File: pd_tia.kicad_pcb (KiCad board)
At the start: 2 copper layers, 75.1 x 65.2 mm, 21 parts, among them P1 BNC, U1 ED2610, U2 LM2940, U3 OPA2211

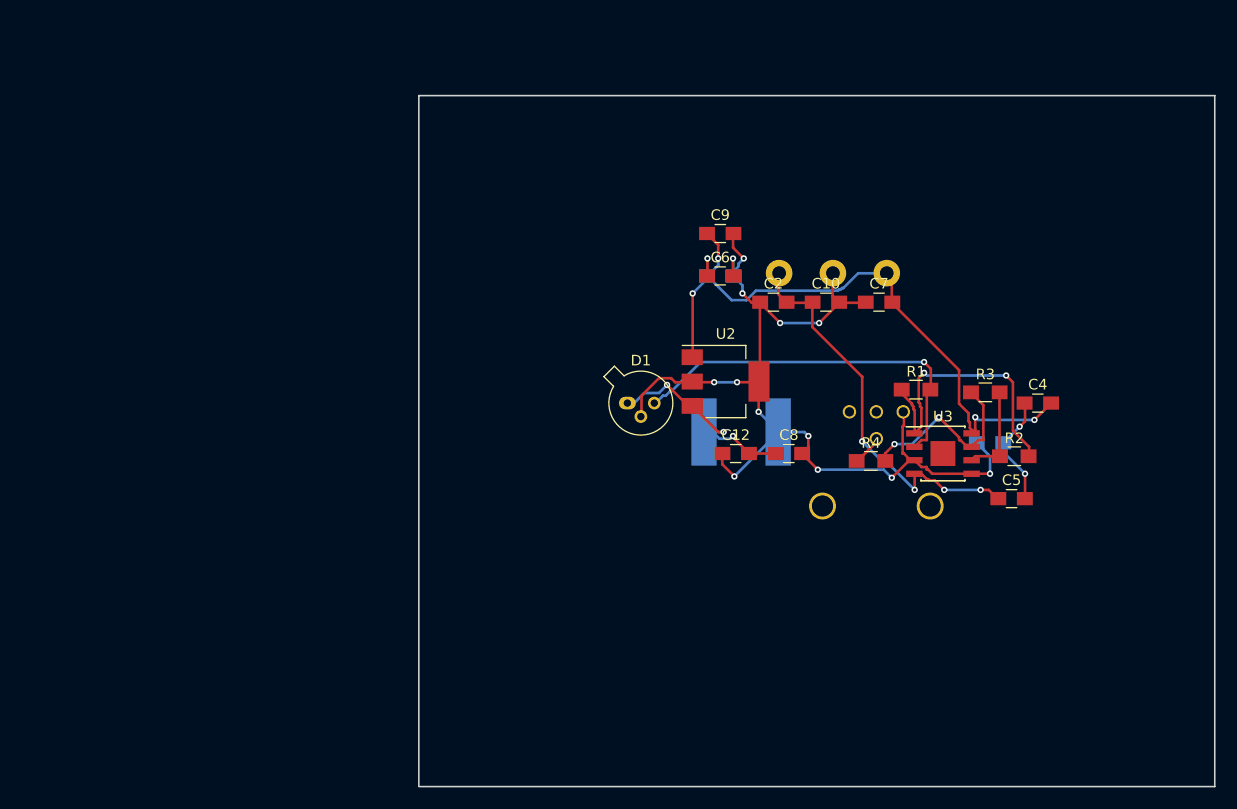
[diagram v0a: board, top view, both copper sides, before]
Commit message: Added SMA connector instead of BNC
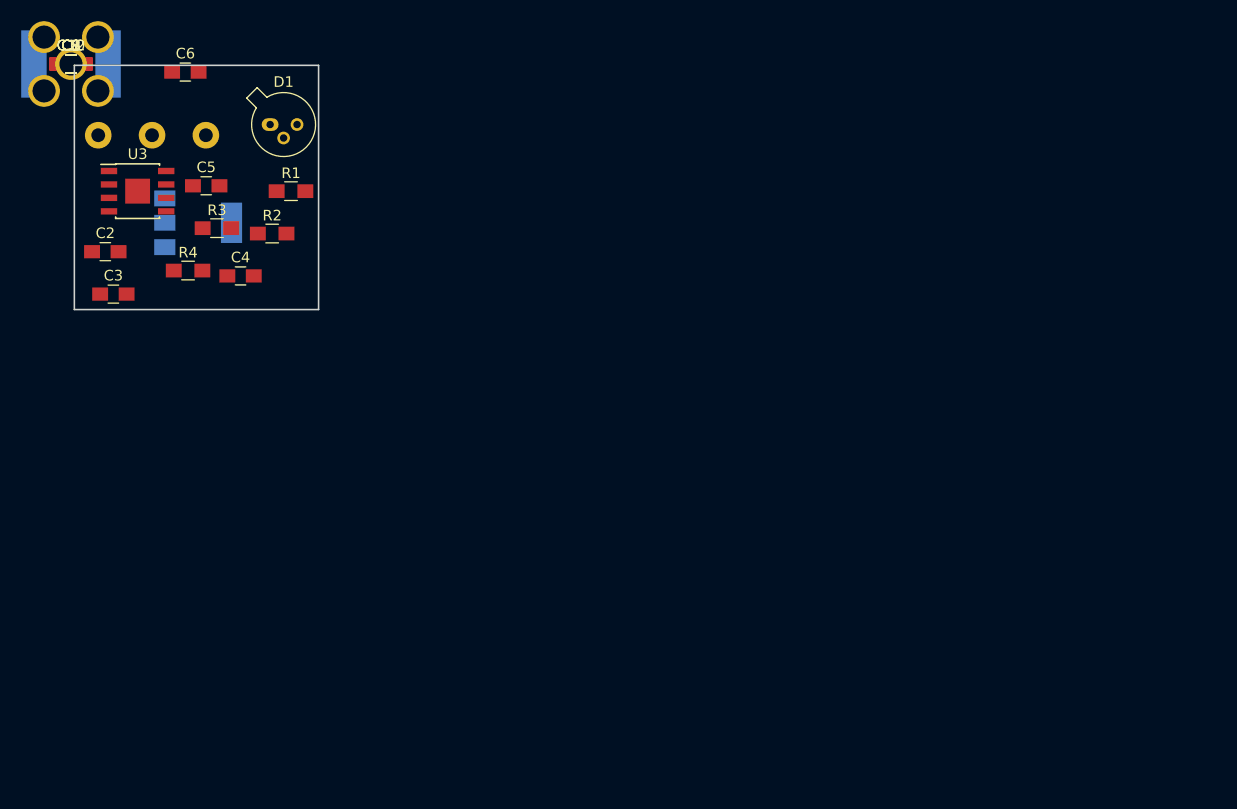
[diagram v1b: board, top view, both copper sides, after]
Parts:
- C1, C3: moved to F.Cu
- P1: footprint footprints:Dual-BNC-ARF2136 -> footprints:SMA_throughhole
- U2: moved to B.Cu
- moved P1 86.7 mm to (110.0, 60.0)
- moved C3 83.9 mm to (114.0, 81.7)
- moved C5 81.5 mm to (122.7, 71.5)
- moved U3 79.9 mm to (116.3, 72.0)
- moved C7 79.5 mm to (110.0, 60.0)
- moved C8 77.1 mm to (110.0, 60.0)
- moved C4 76.2 mm to (126.0, 80.0)
- moved C10 74.7 mm to (110.0, 60.0)
- moved R3 74.2 mm to (123.8, 75.5)
- moved R2 73.1 mm to (129.0, 76.0)
- moved C12 72.7 mm to (110.0, 60.0)
- moved C11 72.2 mm to (110.0, 60.0)
- moved R4 66.9 mm to (121.0, 79.5)
- moved U1 65.6 mm to (118.0, 66.2)
- moved C1 64.5 mm to (110.0, 60.0)
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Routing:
- net GND: track 97.6 -> 0.00 mm, vias 13 -> 0
- net +15V: track 63.8 -> 0.00 mm, vias 5 -> 0
- net -15V: track 38.2 -> 0.00 mm, vias 4 -> 0
- net Net-(D1-Pad3): track 36.4 -> 0.00 mm, vias 1 -> 0
- net Net-(R1-Pad1): track 27.4 -> 0.00 mm, vias 2 -> 0
- net +9V: track 21.6 -> 0.00 mm, vias 3 -> 0
- net Net-(R3-Pad1): track 18.1 -> 0.00 mm, vias 2 -> 0
- net Net-(C3-Pad2): track 10.9 -> 0.00 mm, vias 2 -> 0
- net Net-(R2-Pad1): track 8.99 -> 0.00 mm
- net Net-(P1-Pad1): track 3.08 -> 0.00 mm
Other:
- board size 75.1 x 65.2 mm -> 23.1 x 23.1 mm

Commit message: First shot at layout... almost all components in
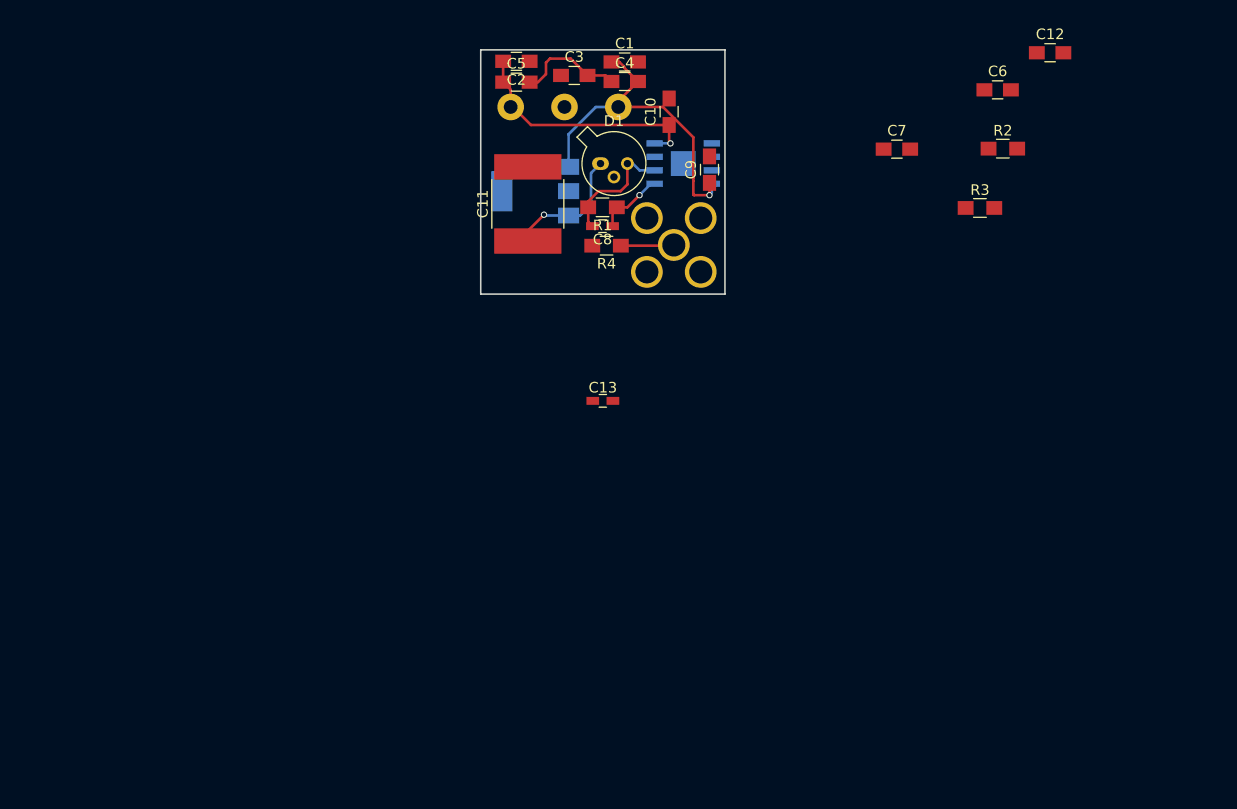
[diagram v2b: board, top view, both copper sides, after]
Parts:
- added C13: 15pF, Capacitors_SMD:C_0603_HandSoldering, F.Cu at (160.2, 91.8)
- C11: moved to F.Cu
- C8: value 0.1uF -> 15pF; footprint Capacitors_SMD:C_0805_HandSoldering -> Capacitors_SMD:C_0603_HandSoldering
- U3: moved to B.Cu
- moved C12 92.4 mm to (202.4, 58.9)
- moved C7 78.4 mm to (187.9, 68.0)
- moved C6 76.7 mm to (197.4, 62.4)
- moved R3 72.0 mm to (195.8, 73.6)
- moved R2 69.4 mm to (197.9, 68.0)
- moved C9 61.1 mm to (170.2, 70.0), turned to 90 degrees
- moved P1 59.4 mm to (166.9, 77.1)
- moved C10 56.6 mm to (166.4, 64.5), turned to 90 degrees
- moved C8 52.4 mm to (160.1, 75.3), turned to 180 degrees
- moved C1 52.3 mm to (162.2, 59.8)
- moved U3 51.6 mm to (167.8, 69.4)
- moved C3 48.1 mm to (157.5, 61.1)
- moved C11 45.1 mm to (153.1, 73.2), turned to 90 degrees
- moved C2 42.8 mm to (152.0, 59.8), turned to 180 degrees
- moved C4 40.6 mm to (162.2, 61.7)
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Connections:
- C8 pad 1: +9V -> Net-(C8-Pad1)
- C8 pad 2: GND -> Net-(C8-Pad2)
- D1 pad 3: Net-(D1-Pad3) -> Net-(C8-Pad2)
- R1 pad 1: Net-(R1-Pad1) -> Net-(C8-Pad1)
- R1 pad 2: Net-(D1-Pad3) -> Net-(C8-Pad2)
- R2 pad 2: Net-(R1-Pad1) -> Net-(C8-Pad1)
- U3 pad 1: Net-(R1-Pad1) -> Net-(C8-Pad1)
- U3 pad 2: Net-(D1-Pad3) -> Net-(C8-Pad2)
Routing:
- net +15V: track 0.00 -> 33.6 mm, vias 0 -> 1
- net -15V: track 0.00 -> 23.5 mm, vias 0 -> 1
- net +9V: track 0.00 -> 12.3 mm, vias 0 -> 1
- net Net-(C8-Pad2): track 0.00 -> 11.7 mm
- net Net-(C3-Pad2): track 0.00 -> 10.2 mm
- net Net-(C8-Pad1): track 0.00 -> 6.43 mm, vias 0 -> 1
- net Net-(P1-Pad1): track 0.00 -> 5.03 mm

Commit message: Almost done. Not quite fitting on board
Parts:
- removed C6: 10uF, Capacitors_SMD:C_0805_HandSoldering
- moved C12 51.9 mm to (154.7, 79.4)
- moved C7 34.2 mm to (153.7, 66.9)
- moved R2 31.2 mm to (167.8, 59.8), turned to 180 degrees
- moved C13 30.2 mm to (170.8, 63.6), turned to 90 degrees
- moved R3 28.8 mm to (168.9, 63.2), turned to 90 degrees
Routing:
- net Net-(C13-Pad1): track 0.00 -> 36.2 mm, vias 0 -> 4
- net GND: track 0.00 -> 28.5 mm, vias 0 -> 4
- net Net-(C8-Pad1): track 6.43 -> 24.3 mm, vias 1 -> 4
- net Net-(C13-Pad2): track 0.00 -> 15.0 mm, vias 0 -> 1
- net +9V: track 12.3 -> 16.2 mm
- net +15V: track 33.6 -> 35.6 mm, vias 1 -> 2
- added copper zone on B.Cu, net GND
- added copper zone on F.Cu, net GND
